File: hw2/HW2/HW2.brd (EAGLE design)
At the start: 50 x 50 mm, 22 parts, among them J1 USB-MB-H

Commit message: Working on .brd
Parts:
- moved R2 20.7 mm to (47.0, 6.35)
- moved R1 15.5 mm to (36.8, 11.4)
- moved R4 6.84 mm to (36.8, 43.2)
- moved R3 3.81 mm to (10.2, 8.89)
- moved USER 3.81 mm to (6.35, 8.89)
- moved C2 1.27 mm to (31.8, 38.1)
- moved C5 1.27 mm to (34.3, 19.1)
- moved U$1 1.27 mm to (16.5, 41.9)
- moved LED1 1.27 mm to (35.6, 2.54)
- moved LED2 1.27 mm to (43.2, 2.54)
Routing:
- net +5V: track 5.34 -> 78.1 mm
- net A4/LED: track 0.00 -> 65.9 mm
- net +3V3: track 41.7 -> 98.2 mm
- net MCLR: track 6.99 -> 34.5 mm
- net B9: track 0.00 -> 27.2 mm
- net B8: track 0.00 -> 27.2 mm
- net B7: track 0.00 -> 27.2 mm
- net N$1: track 0.00 -> 10.9 mm
- net B4/USER: track 49.9 -> 40.1 mm
- net N$2: track 0.00 -> 5.08 mm
- net N$3: track 0.00 -> 2.54 mm
- net N$11: track 5.08 -> 3.81 mm

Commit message: Finished .brd wiring
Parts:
- J2: device HW2:1X05 -> HW2:1X06
- moved RESET 9.92 mm to (48.3, 39.4), turned to 180 degrees
- moved C1 8.13 mm to (12.7, 14.0), turned to 90 degrees
- moved R4 5.39 mm to (40.6, 39.4)
- moved J2 1.27 mm to (48.9, 48.3), turned to 180 degrees
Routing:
- net +3V3: track 98.2 -> 147.7 mm, vias 0 -> 1
- net USBID: track 0.00 -> 49.1 mm, vias 0 -> 2
- net D-: track 0.00 -> 44.4 mm
- net D+: track 0.00 -> 38.0 mm
- net PGC: track 0.00 -> 34.3 mm
- net PGD: track 0.00 -> 31.4 mm, vias 0 -> 1
- net MCLR: track 34.5 -> 44.1 mm, vias 0 -> 3
- net GND: track 0.00 -> 6.72 mm
- net +5V: vias 0 -> 1

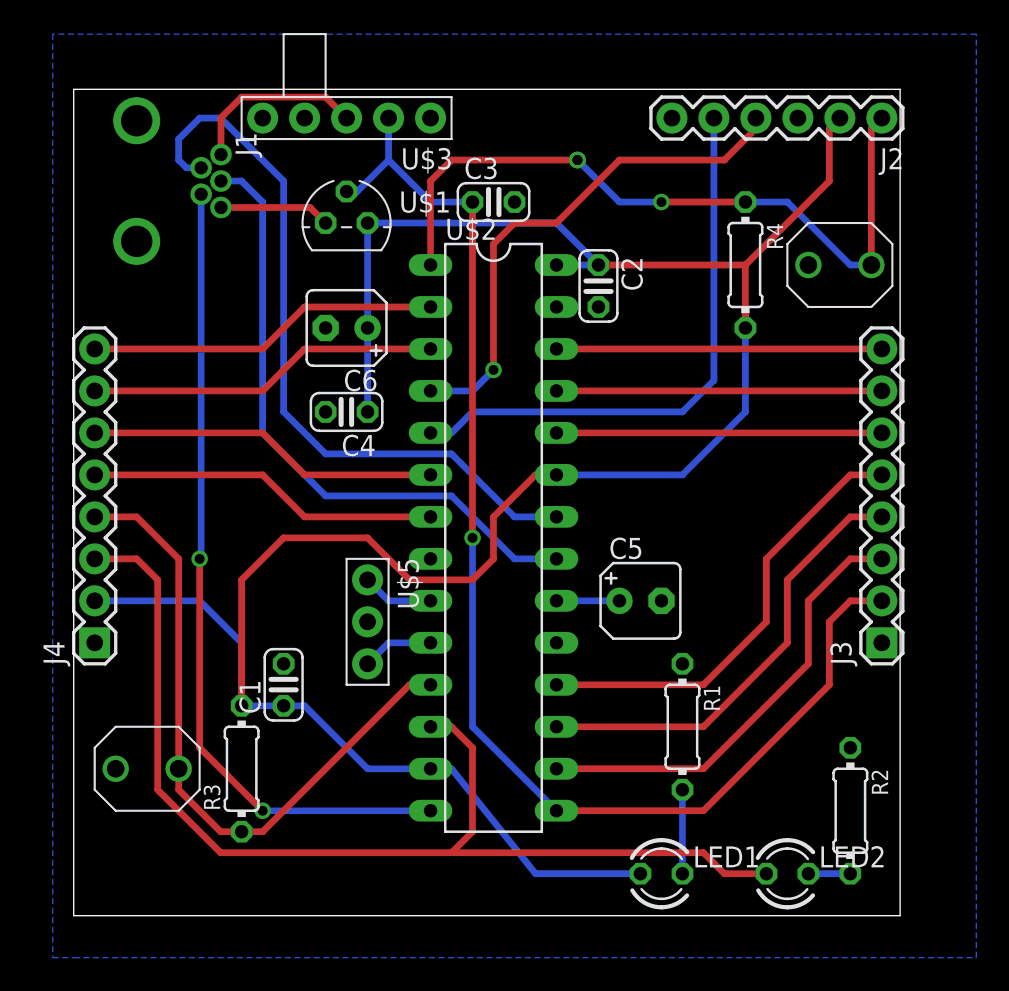
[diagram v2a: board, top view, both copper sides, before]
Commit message: Finished .brd
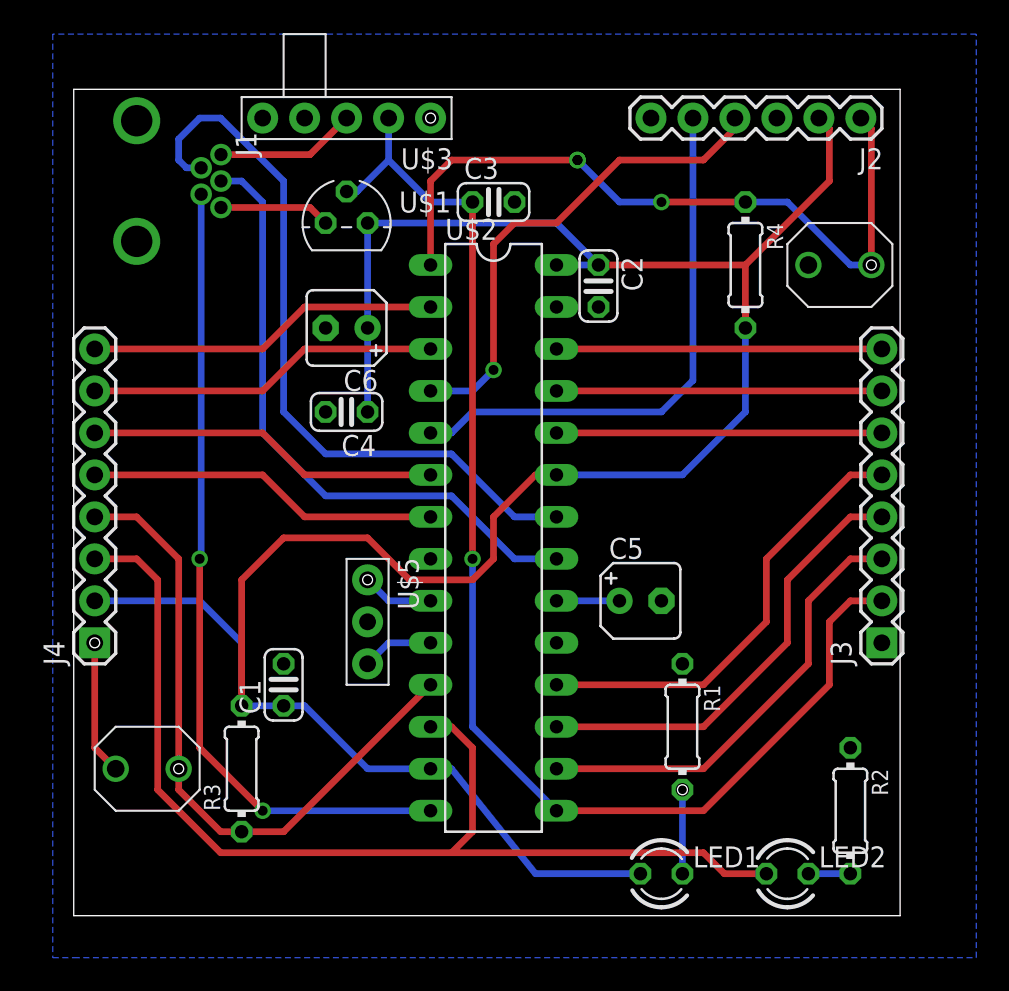
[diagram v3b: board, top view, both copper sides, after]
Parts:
- moved J2 1.27 mm to (47.6, 48.3)
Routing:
- net GND: track 6.72 -> 14.9 mm
- net N$1: track 10.9 -> 8.52 mm
- net PGD: track 31.4 -> 30.1 mm
- net PGC: track 34.3 -> 33.1 mm
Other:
- board text added: "A0 A1 B2 B3 B4 A4 3.3V GND"
- board text added: "B15 B14 B13 B9 B8 B7 5V GND"
- board text added: "RESET"
- board text added: "USER"
